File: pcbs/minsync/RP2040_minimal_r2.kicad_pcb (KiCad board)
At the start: 2 copper layers, 42 x 42 mm, 45 parts, among them J1 SWD_JST, J5 SWD_HEADERS, J6 Conn_01x01_Pin, J7 SSD1306, SW1 SW_Push, U1 NCP1117-3.3_SOT223, U2 W25Q128JVS, U3 RP2040, U4 Si5351A-B-GT, Y2 Crystal_GND24

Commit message: Try new pitopi connector
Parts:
- PTP1, PTP2, PTP3, PTP4: value Comm -> BM23FR0.6-6DS-0.35V_51_; footprint RP2040_minimal:pitopi_and_power -> RP2040_minimal:HRS_BM23FR0.6-6DS-0.35V_51_
- moved PTP1 0.50 mm to (100.0, 83.0), turned to 180 degrees
- moved PTP2 0.50 mm to (83.0, 100.0), turned to -90 degrees
- moved PTP3 0.50 mm to (100.0, 117.0), turned to 0 degrees
- moved PTP4 0.50 mm to (117.0, 100.2), turned to 90 degrees
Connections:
- PTP1 pad 1: GND -> /GPIO0
- PTP1 pad 2: VBUS -> /GPIO5
- PTP1 pad 3: /GPIO5 -> /GPIO1
- PTP1 pad 4: /GPIO2 -> /GPIO4
- PTP1 pad 5: /GPIO4 -> /GPIO2
- PTP1 pad 6: /GPIO1 -> /GPIO3
- PTP2 pad 1: GND -> /GPIO6
- PTP2 pad 2: VBUS -> /GPIO11
- PTP2 pad 3: /GPIO11 -> /GPIO7
- PTP2 pad 4: /GPIO8 -> /GPIO10
- PTP2 pad 5: /GPIO10 -> /GPIO8
- PTP2 pad 6: /GPIO7 -> /GPIO9
- PTP3 pad 1: GND -> /GPIO19
- PTP3 pad 2: VBUS -> /GPIO18
- PTP3 pad 4: /GPIO22 -> /GPIO17
- PTP3 pad 5: /GPIO18 -> /GPIO22
- PTP3 pad 6: /GPIO19 -> /GPIO16
- PTP4 pad 1: GND -> /GPIO27_ADC1
- PTP4 pad 2: VBUS -> /GPIO26_ADC0
- PTP4 pad 4: /GPIO29_ADC3 -> /GPIO24
- PTP4 pad 5: /GPIO26_ADC0 -> /GPIO29_ADC3
- PTP4 pad 6: /GPIO27_ADC1 -> /GPIO23
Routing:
- net VBUS: track 139.7 -> 2.93 mm
- net /GPIO28_ADC2: track 13.5 -> 19.6 mm
- net /GPIO17: track 22.4 -> 16.5 mm
- net /GPIO21: track 18.7 -> 23.8 mm
- net /GPIO6: track 19.6 -> 24.5 mm
- net /GPIO24: track 17.6 -> 13.0 mm
- net /GPIO0: track 31.5 -> 35.6 mm, vias 1 -> 2
- net /GPIO16: track 20.1 -> 16.4 mm
- net /GPIO22: track 24.3 -> 27.9 mm
- net /GPIO29_ADC3: track 17.1 -> 20.6 mm
- net /GPIO9: track 16.4 -> 13.8 mm
- net /GPIO2: track 37.1 -> 34.8 mm, vias 1 -> 2
- net /GPIO23: track 15.2 -> 12.9 mm
- net /GPIO27_ADC1: track 16.5 -> 18.5 mm
- net /GPIO7: track 21.9 -> 23.6 mm
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
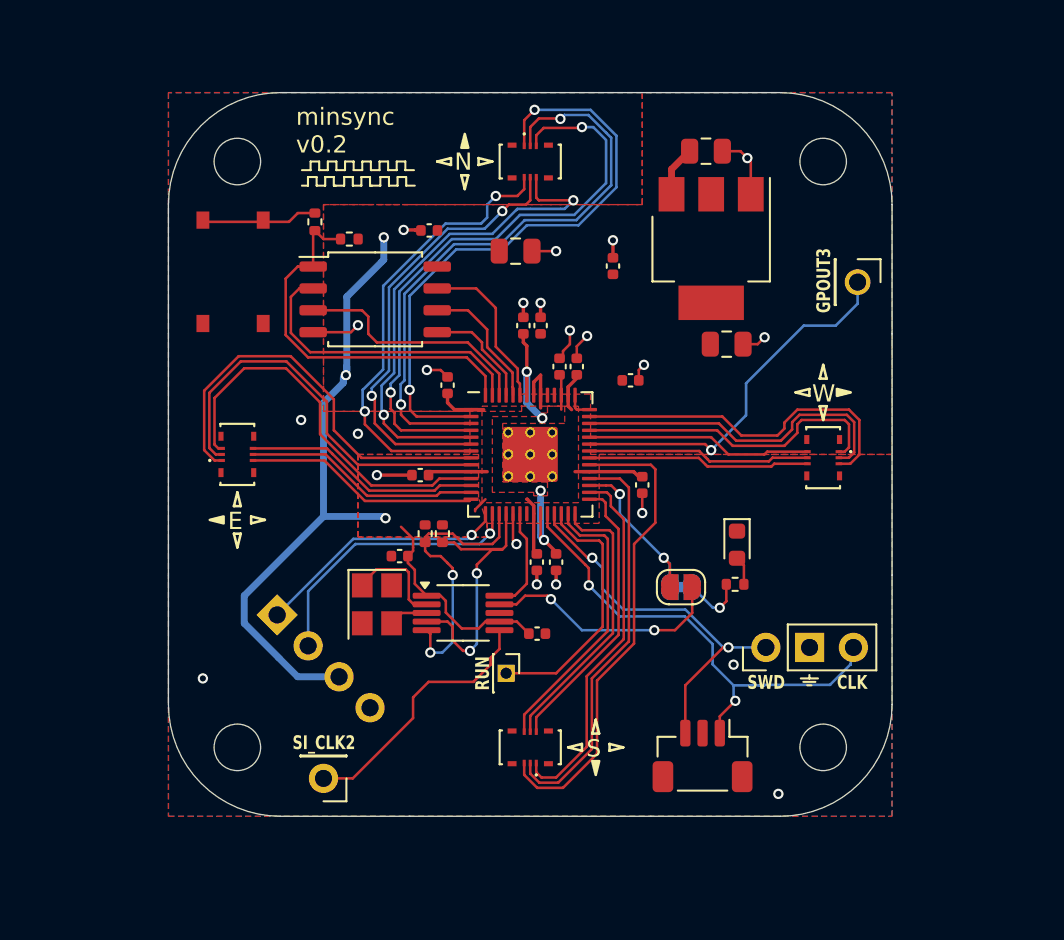
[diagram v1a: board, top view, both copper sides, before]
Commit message: Use JST SH headers for pitopi
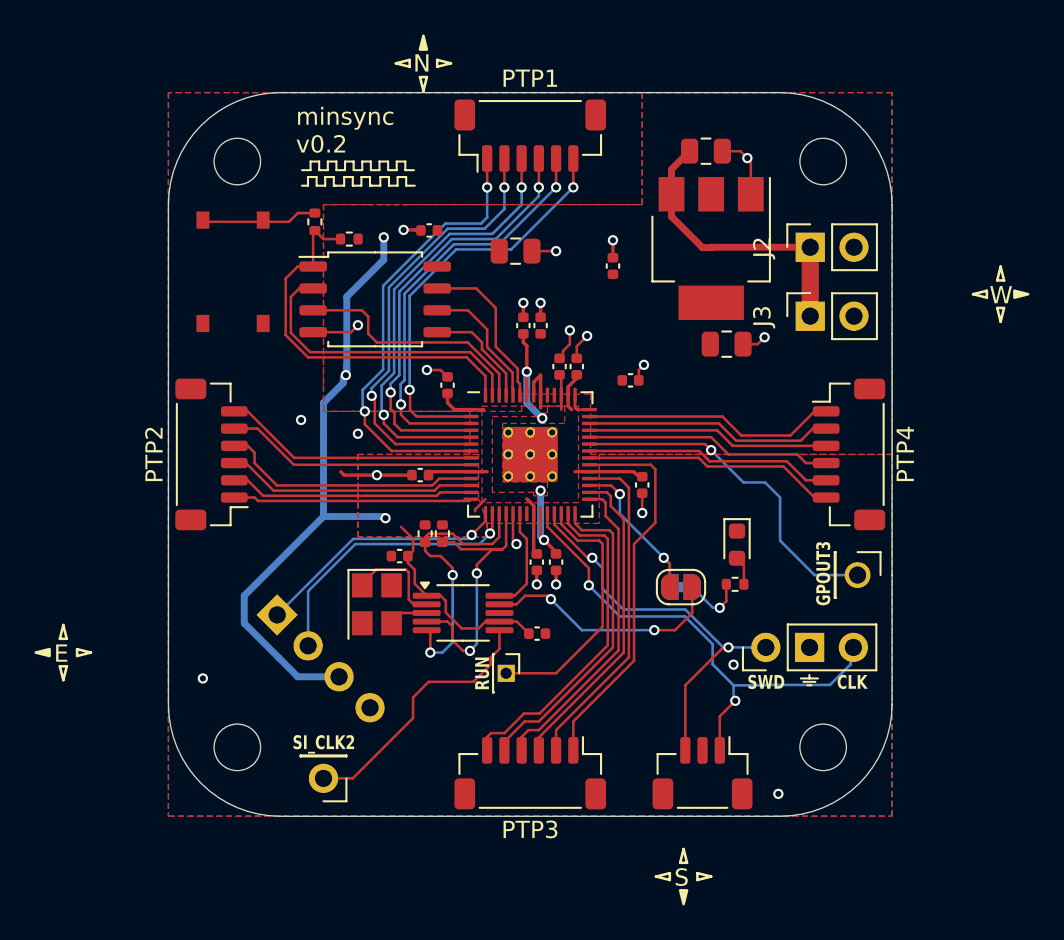
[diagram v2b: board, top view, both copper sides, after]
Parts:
- added J2: POWER, Connector_PinSocket_2.54mm:PinSocket_1x02_P2.54mm_Vertical, F.Cu at (116.2, 88.0)
- added J3: POWER, Connector_PinSocket_2.54mm:PinSocket_1x02_P2.54mm_Vertical, F.Cu at (116.2, 92.0)
- PTP1, PTP2, PTP3, PTP4: footprint RP2040_minimal:HRS_BM23FR0.6-6DS-0.35V_51_ -> Connector_JST:JST_SH_BM06B-SRSS-TB_1x06-1MP_P1.00mm_Vertical
- moved TP1 17.0 mm to (119.0, 107.0)
- moved PTP4 1.51 mm to (118.5, 100.0), turned to -90 degrees
- moved PTP1 1.50 mm to (100.0, 81.5), turned to 0 degrees
- moved PTP2 1.50 mm to (81.5, 100.0), turned to 90 degrees
- moved PTP3 1.50 mm to (100.0, 118.5), turned to 180 degrees
- moved J1 1.00 mm to (110.0, 118.5)
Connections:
- PTP1 pad 1: /GPIO0 -> /GPIO5
- PTP1 pad 2: /GPIO5 -> /GPIO4
- PTP1 pad 3: /GPIO1 -> /GPIO3
- PTP1 pad 4: /GPIO4 -> /GPIO2
- PTP1 pad 5: /GPIO2 -> /GPIO1
- PTP1 pad 6: /GPIO3 -> /GPIO0
- PTP2 pad 1: /GPIO6 -> /GPIO11
- PTP2 pad 2: /GPIO11 -> /GPIO10
- PTP2 pad 3: /GPIO7 -> /GPIO9
- PTP2 pad 4: /GPIO10 -> /GPIO8
- PTP2 pad 5: /GPIO8 -> /GPIO7
- PTP2 pad 6: /GPIO9 -> /GPIO6
- PTP3 pad 1: /GPIO19 -> /GPIO22
- PTP3 pad 2: /GPIO18 -> /GPIO21
- PTP3 pad 3: /GPIO21 -> /GPIO19
- PTP3 pad 4: /GPIO17 -> /GPIO18
- PTP3 pad 5: /GPIO22 -> /GPIO17
- PTP4 pad 1: /GPIO27_ADC1 -> /GPIO29_ADC3
- PTP4 pad 2: /GPIO26_ADC0 -> /GPIO28_ADC2
- PTP4 pad 3: /GPIO28_ADC2 -> /GPIO27_ADC1
- PTP4 pad 4: /GPIO24 -> /GPIO26_ADC0
- PTP4 pad 5: /GPIO29_ADC3 -> /GPIO24
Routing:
- net VBUS: track 2.93 -> 17.0 mm
- net /GPIO0: track 35.6 -> 24.1 mm
- net /GPIO1: track 35.4 -> 24.4 mm
- net /GPIO2: track 34.8 -> 25.1 mm
- net /GPIO6: track 24.5 -> 14.9 mm
- net /GPIO7: track 23.6 -> 14.6 mm
- net /GPIO8: track 22.9 -> 15.2 mm
- net /GPIO29_ADC3: track 20.6 -> 14.8 mm
- net /GPIO22: track 27.9 -> 22.2 mm
- net /GPIO28_ADC2: track 19.6 -> 14.4 mm
- net /GPIO27_ADC1: track 18.5 -> 14.1 mm
- net /GPIO21: track 23.8 -> 19.5 mm
- net /GPIO3: track 29.5 -> 25.6 mm
- net /GPIO19: track 21.4 -> 18.4 mm
- net /GPIO16: track 16.4 -> 19.4 mm
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
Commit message: Add vias before JST connectors
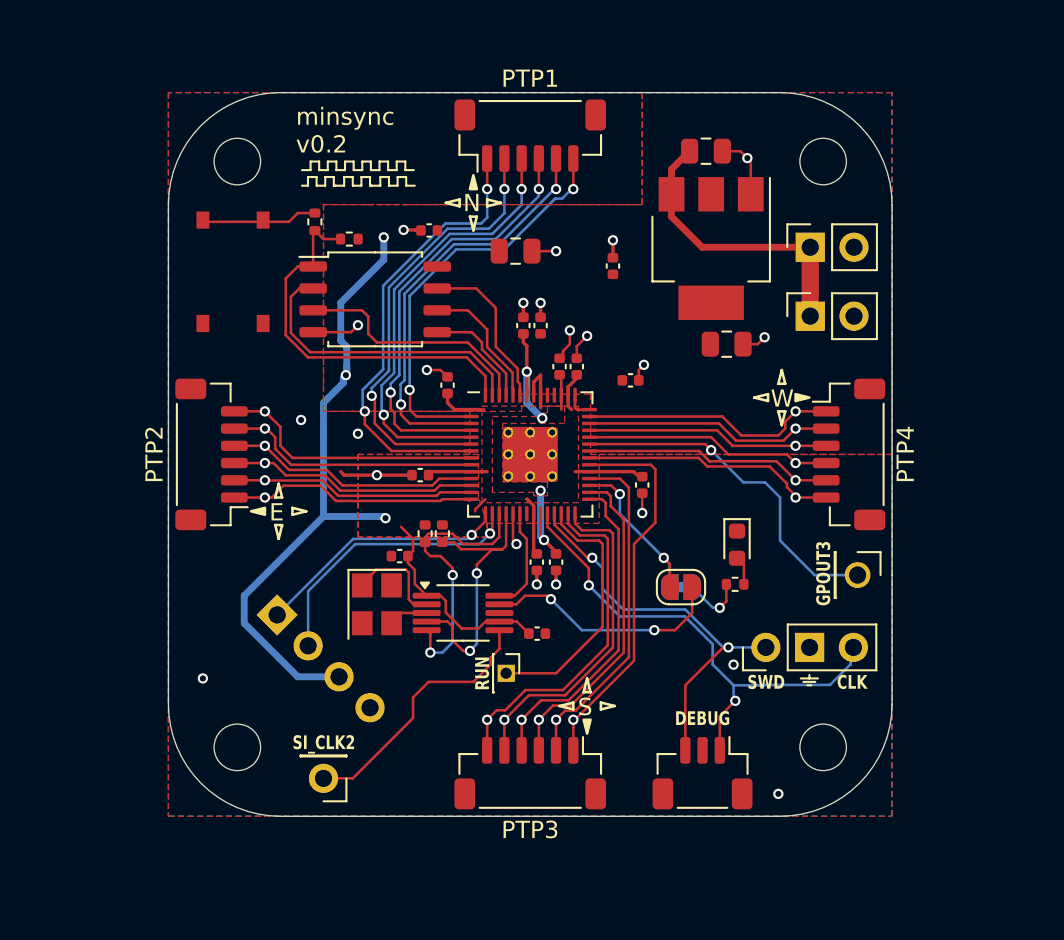
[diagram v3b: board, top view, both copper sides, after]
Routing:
- net /GPIO17: track 18.7 -> 19.9 mm, vias 0 -> 1
- net /GPIO29_ADC3: track 14.8 -> 15.7 mm, vias 0 -> 1
- net /GPIO23: track 14.7 -> 15.5 mm, vias 0 -> 1
- net /GPIO11: track 13.9 -> 14.6 mm, vias 0 -> 1
- net /GPIO19: track 18.4 -> 19.0 mm, vias 0 -> 1
- net /GPIO18: track 18.4 -> 19.0 mm, vias 0 -> 1
- net /GPIO16: track 19.4 -> 20.0 mm, vias 0 -> 1
- net /GPIO9: track 14.5 -> 15.1 mm, vias 0 -> 1
- net /GPIO6: track 14.9 -> 15.4 mm, vias 0 -> 1
- net /GPIO7: track 14.6 -> 15.0 mm, vias 0 -> 1
- net /GPIO21: track 19.5 -> 19.9 mm, vias 0 -> 1
- net /GPIO8: track 15.2 -> 14.9 mm, vias 0 -> 1
- net /GPIO22: track 22.2 -> 22.3 mm, vias 0 -> 1
- net /GPIO26_ADC0: vias 0 -> 1
- net /GPIO24: vias 0 -> 1
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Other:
- board text added: "DEBUG"

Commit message: Update TODO's for minsync v0.2
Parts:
- removed J2: POWER, Connector_PinSocket_2.54mm:PinSocket_1x02_P2.54mm_Vertical
- J3: footprint Connector_PinSocket_2.54mm:PinSocket_1x02_P2.54mm_Vertical -> Connector_PinHeader_2.54mm:PinHeader_1x02_P2.54mm_Vertical
- moved J3 4.71 mm to (118.8, 88.0), turned to -90 degrees
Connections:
- J3 pad 1: VBUS -> GND
- J3 pad 2: GND -> VBUS
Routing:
- net VBUS: track 17.0 -> 13.2 mm
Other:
- board text added: "+5V"
- board text added: "GND"

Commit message: Productionize minsync v0.2
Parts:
- C2, C3: footprint Capacitor_SMD:C_0402_1005Metric -> Capacitor_SMD:C_0603_1608Metric
- moved R4 7.60 mm to (94.0, 112.2), turned to -90 degrees
- moved R5 7.60 mm to (95.0, 112.2), turned to -90 degrees
- moved C2 2.07 mm to (94.4, 106.5), turned to 0 degrees
- moved C15 1.39 mm to (105.1, 96.9)
- moved J6 1.36 mm to (99.9, 112.3), turned to 0 degrees
- moved C3 0.60 mm to (100.9, 110.1)
- turned Y2 to 90 degrees
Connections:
- Y2 pad 1: /XA -> /XB
- Y2 pad 3: /XB -> /XA
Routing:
- net +3V3: track 71.1 -> 76.0 mm
- net /GPIO15: track 16.5 -> 13.9 mm
- net /GPIO14: track 16.2 -> 13.9 mm
- net GND: track 27.5 -> 29.3 mm, vias 22 -> 21
- net /RUN: track 15.0 -> 13.3 mm
- net /GPIO29_ADC3: track 15.7 -> 14.5 mm
- net /GPIO13: track 16.3 -> 17.1 mm
- net /GPIO28_ADC2: track 14.4 -> 13.9 mm
- net /GPIO11: track 14.6 -> 14.0 mm
